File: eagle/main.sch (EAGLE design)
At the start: 15 parts, among them Q1 IRF540, Q2 IRF540

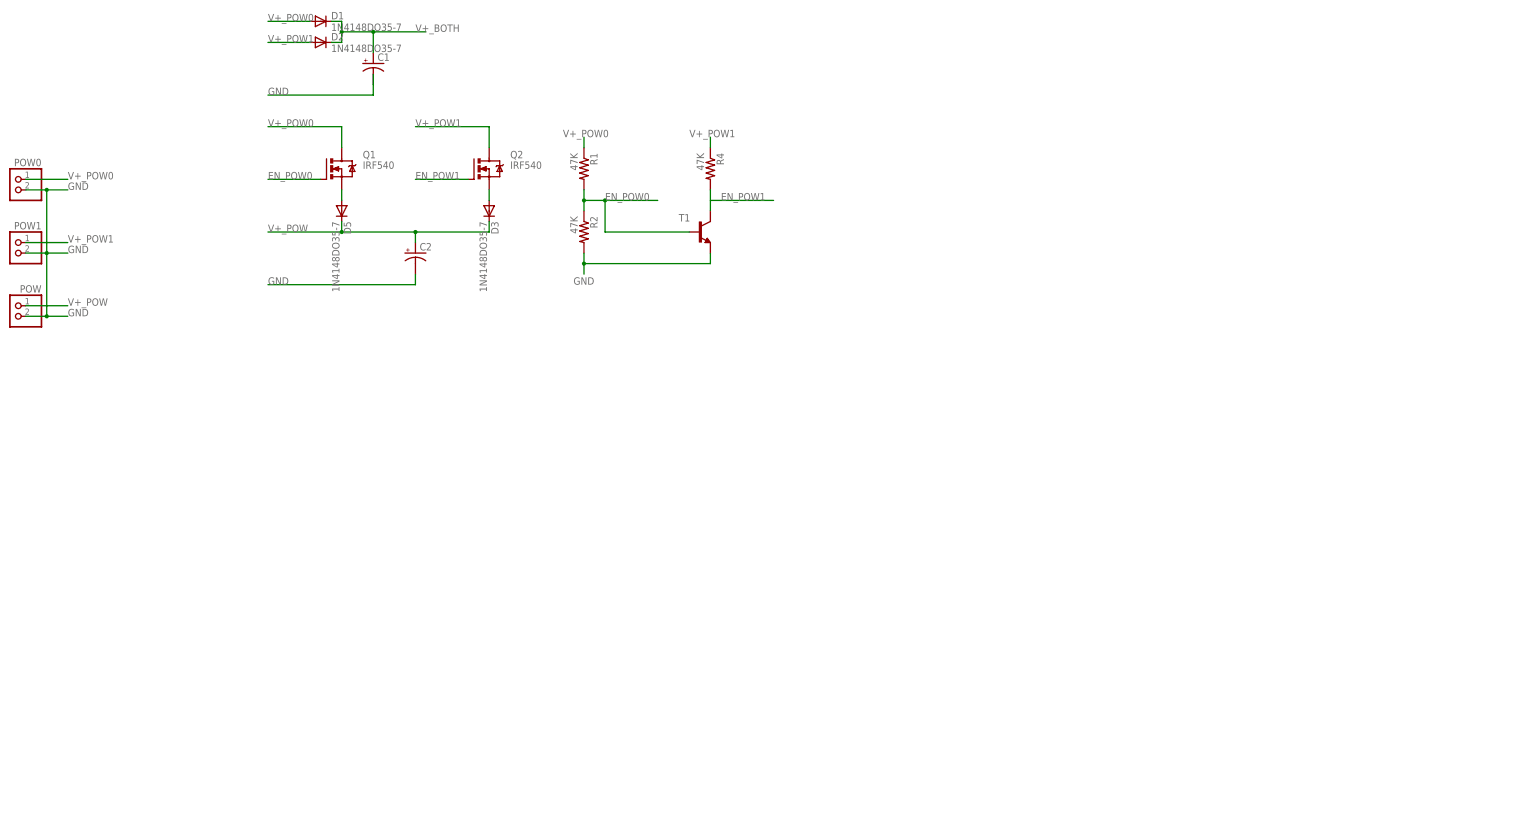
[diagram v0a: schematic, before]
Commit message: update schematic
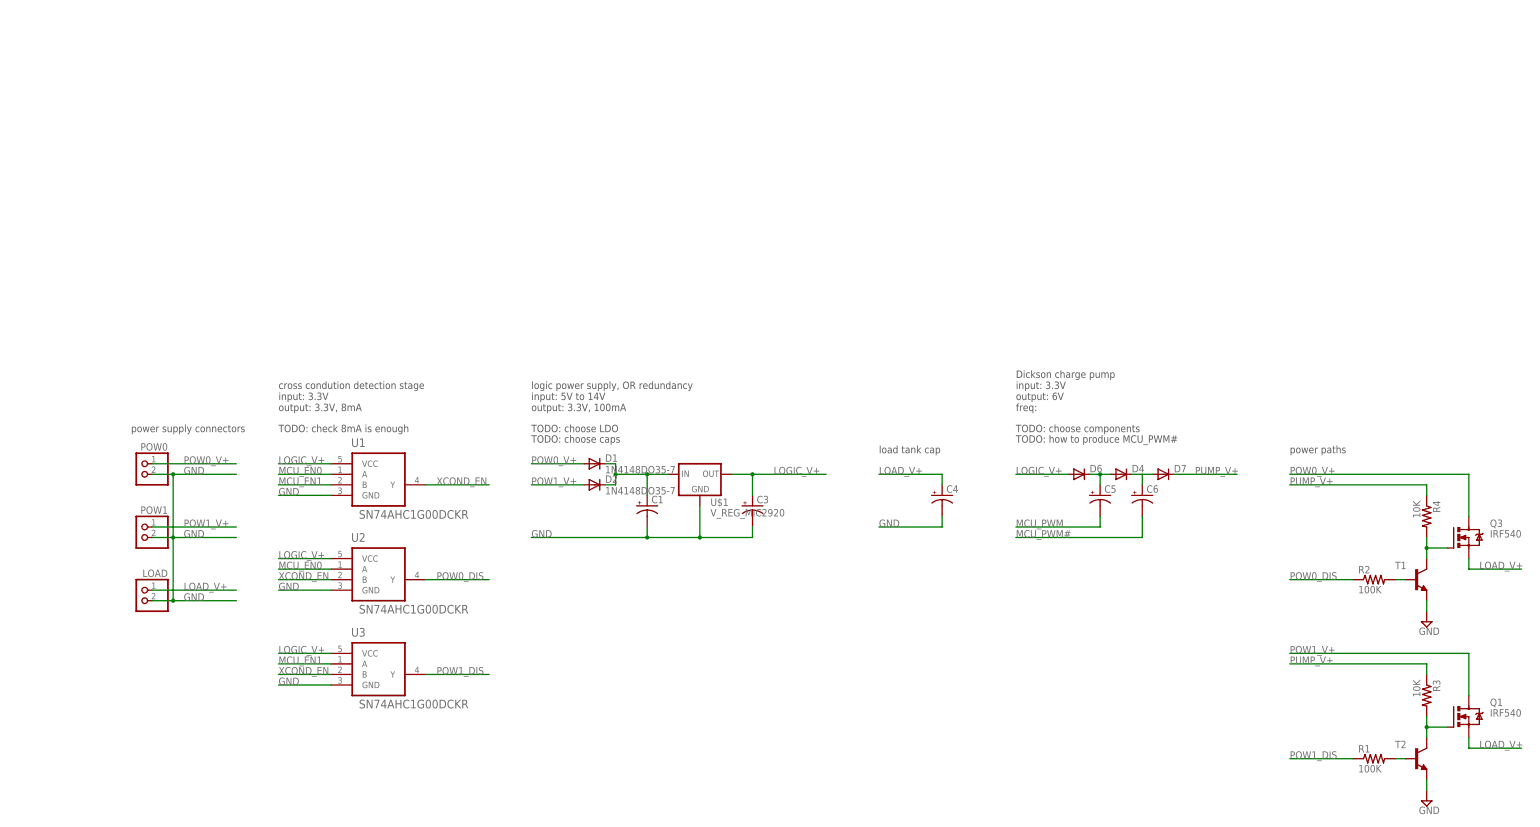
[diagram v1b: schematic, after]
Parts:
- removed C2: (no value), rcl:CPOL-US085CS-1AR
- removed D3, D5: 1N4148DO35-7, diode:1N4148DO35-7
- removed POW: (no value), pinhead:PINHD-1X2
- removed Q2: IRF540, transistor-power:IRF540
- added C3, C4, C5, C6: (no value), rcl:CPOL-US085CS-1AR
- added D4, D6, D7: 1N4148DO35-7, diode:1N4148DO35-7
- added LOAD: (no value), pinhead:PINHD-1X2
- added Q3: IRF540, transistor-power:IRF540
- added R3: 10K, resistor:R-US_0204/2V
- added T2: (no value), transistor:-NPN-TO92
- added U$1: V_REG_MIC2920, SparkFun:V_REG_MIC2920
- added U1, U2, U3: SN74AHC1G00DCKR, TI-SN74AHC1G00DCKR@E:SN74AHC1G00DCKR
- R1, R2: value 47K -> 100K
- R4: value 47K -> 10K
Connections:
- removed net EN_POW0: Q1.G, R1.2, R2.1, T1.B
- removed net EN_POW1: Q2.G
- removed net V+_POW: C2.+, D3.C, D5.C, POW.1
- removed net V+_POW0: D1.A, POW0.1, Q1.D, R1.1
- removed net V+_POW1: D2.A, POW1.1, Q2.D, R4.1
- new net LOAD_V+: C4.+, LOAD.1, Q1.S, Q3.S
- new net LOGIC_V+: C3.+, D6.A, U$1.OUT, U1.VCC, U2.VCC, U3.VCC
- new net MCU_EN0: U1.A, U2.A
- new net MCU_EN1: U1.B, U3.A
- new net MCU_PWM: C5.-
- new net MCU_PWM#: C6.-
- new net N$4: C5.+, D4.A, D6.C
- new net N$5: C6.+, D4.C, D7.A
- new net N$6: R2.2, T1.B
- new net POW0_DIS: R2.1, U2.Y
- new net POW0_V+: D1.A, POW0.1, Q3.D
- new net POW1_DIS: R1.1, U3.Y
- new net POW1_V+: D2.A, POW1.1, Q1.D
- new net PUMP_V+: D7.C, R3.1, R4.1
- new net XCOND_EN: U1.Y, U2.B, U3.B
- net GND: now also C3.-, C4.-, LOAD.2, T2.E, U$1.GND, U1.GND, U2.GND, U3.GND; no longer C2.-, POW.2, R2.2
- net N$1: now also Q3.G
- net N$2: now also Q1.G, R3.2, T2.C; no longer D5.A, Q1.S
- net N$3: now also R1.2, T2.B; no longer D3.A, Q2.S
- net V+_BOTH: now also U$1.IN
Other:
- note added: "Dickson charge pump input: 3.3V output: 6V freq:"
- note added: "TODO: check 8mA is enough"
- note added: "TODO: choose LDO"
- note added: "TODO: choose caps"
- note added: "TODO: choose components"
- note added: "TODO: how to produce MCU_PWM#"
- note added: "cross condution detection stage input: 3.3V output: 3.3V, 8mA"
- note added: "load tank cap"
- note added: "logic power supply, OR redundancy input: 5V to 14V output: 3.3V, 100mA"
- note added: "power paths"
- note added: "power supply connectors"
- moved on the sheet: C1, D1, D2, POW0, POW1, Q1, R1, R2, R4, T1

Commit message: update schematics
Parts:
- added D3: 1N4148DO35-7, diode:1N4148DO35-7
- added R5, R7: 50K, resistor:R-US_0204/2V
- added R6, R8: 10K, resistor:R-US_0204/2V
- added SPI_CON: (no value), pinhead:PINHD-1X6
- added U$2: TEENSY_3.0_ALLPINS, Teensy3.0:TEENSY_3.0_ALLPINS
- renumbered LOAD to LOAD_CON, POW0 to POW0_CON, POW1 to POW1_CON
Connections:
- net MCU_PWM# renamed PUMP_PWM#
- removed net MCU_PWM: C5.-
- removed net V+_BOTH: C1.+, D1.C, D2.C, U$1.IN
- new net MCU_ADC0: U$2.15/A1
- new net MCU_ADC1: U$2.16/A2
- new net MCU_V+: U$2.3.3V, U1.VCC, U2.VCC, U3.VCC
- new net POW01_V+: C1.+, D1.C, D2.C, D6.A, U$1.IN
- new net POW0_VMON: R5.2, R6.1, U$2.11, U$2.23/A9, U$2.3
- new net POW1_VMON: R7.2, R8.1, U$2.12, U$2.4, U$2.9
- new net PUMP_PWM: C5.-, U$2.22/A8
- new net SPI_CS: SPI_CON.2, U$2.2
- new net SPI_MISO: SPI_CON.3, U$2.8
- new net SPI_MOSI: SPI_CON.4, U$2.7
- new net SPI_SCK: SPI_CON.5, U$2.14/A0
- new net SPI_V+: D3.C, SPI_CON.6
- net GND: now also R6.2, R8.2, SPI_CON.1, U$2.GND
- net LOGIC_V+: now also D3.A, U$2.VIN; no longer D6.A, U1.VCC, U2.VCC, U3.VCC
- net POW0_DIS: now also U$2.0
- net POW0_V+: now also R5.1
- net POW1_DIS: now also U$2.1
- net POW1_V+: now also R7.1
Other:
- note added: "Dickson charge pump output: input + 5V freq:"
- note added: "TODO: 6:1 amplifier based stage"
- note added: "TODO: choose diodes"
- note added: "logic power supply, OR redundancy input: 5V to 14V output: 3.7V, 100mA"
- note added: "voltage monitoring paths"
- note removed: "Dickson charge pump input: 3.3V output: 6V freq:"
- note removed: "logic power supply, OR redundancy input: 5V to 14V output: 3.3V, 100mA"

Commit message: PWM#
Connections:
- net PUMP_PWM#: now also U$2.21/A7
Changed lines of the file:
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@@
 <label x="254" y="-17.78" size="1.778" layer="95"/>
+</segment>
+<segment>
+<pinref part="U$2" gate="G$1" pin="21/A7"/>
+<wire x1="226.06" y1="-121.92" x2="243.84" y2="-121.92" width="0.1524" layer="91"/>
+<label x="228.6" y="-121.92" size="1.778" layer="95"/>
 </segment>
 </net>

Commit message: update schematics
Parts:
- removed U$1: V_REG_MIC2920, SparkFun:V_REG_MIC2920
- added C2: 470p, resistor:C-EU025-024X044
- added IC1: TS5205, v-reg:TS5205
- added U6: OPA2340UA, TI-OPA2340UA:OPA2340UA
- C3: value (none) -> 2.2u
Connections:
- new net N$8: C2.1, IC1.CB
- net GND: now also C2.2, IC1.GND; no longer U$1.GND
- net LOGIC_V+: now also IC1.VOUT; no longer U$1.OUT
- net POW01_V+: now also IC1.CE, IC1.VIN; no longer U$1.IN
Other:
- note added: "TODO: 5:1 amplifier based stage"
- note added: "TODO: choose LDO 4V"
- note added: "logic power supply, OR redundancy input: 5V to 16V output: 4V, 150mA"
- note removed: "TODO: 6:1 amplifier based stage"
- note removed: "TODO: choose LDO"
- note removed: "logic power supply, OR redundancy input: 5V to 14V output: 3.7V, 100mA"
- moved on the sheet: C1, C3, C4, D3
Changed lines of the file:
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@@
 <part name="U2" library="TI-SN74AHC1G00DCKR@E" deviceset="SN74AHC1G00DCKR" device=""/>
 <part name="U3" library="TI-SN74AHC1G00DCKR@E" deviceset="SN74AHC1G00DCKR" device=""/>
-<part name="U$1" library="SparkFun" deviceset="V_REG_MIC2920" device=""/>
-<part name="C3" library="rcl" deviceset="CPOL-US" device="085CS-1AR"/>
+<part name="C3" library="rcl" deviceset="CPOL-US" device="085CS-1AR" value="2.2u"/>
 <part name="C4" library="rcl" deviceset="CPOL-US" device="085CS-1AR"/>
 <part name="D4" library="diode" deviceset="1N4148" device="DO35-7"/>
@@
 <part name="R8" library="resistor" deviceset="R-US_" device="0204/2V" value="10K"/>
 <part name="SUPPLY4" library="supply2" deviceset="GND" device=""/>
+<part name="IC1" library="v-reg" deviceset="TS5205" device=""/>
+<part name="C2" library="resistor" deviceset="C-EU" device="025-024X044" value="470p"/>
+<part name="U6" library="TI-OPA2340UA" deviceset="OPA2340UA" device=""/>
 </parts>
 <sheets>
@@
 <text x="40.64" y="7.62" size="1.778" layer="97">power supply connectors</text>
 <text x="137.16" y="15.24" size="1.778" layer="97">logic power supply, OR redundancy
-input: 5V to 14V
-output: 3.7V, 100mA</text>
-<text x="137.16" y="10.16" size="1.778" layer="97">TODO: choose LDO</text>
+input: 5V to 16V
+output: 4V, 150mA</text>
+<text x="137.16" y="10.16" size="1.778" layer="97">TODO: choose LDO 4V</text>
 <text x="137.16" y="7.62" size="1.778" layer="97">TODO: choose caps</text>
-<text x="220.98" y="2.54" size="1.778" layer="97">load tank cap</text>
+<text x="226.06" y="10.16" size="1.778" layer="97">load tank cap</text>
 <text x="254" y="12.7" size="1.778" layer="97">Dickson charge pump
 output: input + 5V
@@
 <text x="137.16" y="5.08" size="1.778" layer="97">TODO: choose diodes</text>
 <text x="391.16" y="7.62" size="1.778" layer="97">voltage monitoring paths</text>
-<text x="391.16" y="2.54" size="1.778" layer="97">TODO: 6:1 amplifier based stage</text>
+<text x="391.16" y="2.54" size="1.778" layer="97">TODO: 5:1 amplifier based stage</text>
 </plain>
 <instances>
@@
 <attribute name="NAME" x="154.94" y="-4.5974" size="1.778" layer="95"/>
 </instance>
-<instance part="C1" gate="G$1" x="165.1" y="-10.16"/>
+<instance part="C1" gate="G$1" x="162.56" y="-10.16"/>
 <instance part="R2" gate="G$1" x="340.36" y="-27.94"/>
 <instance part="T1" gate="G$1" x="350.52" y="-27.94" smashed="yes">
@@
 <instance part="U2" gate="A" x="93.98" y="-33.02"/>
 <instance part="U3" gate="A" x="93.98" y="-55.88"/>
-<instance part="U$1" gate="G$1" x="177.8" y="-2.54"/>
-<instance part="C3" gate="G$1" x="190.5" y="-10.16"/>
-<instance part="C4" gate="G$1" x="236.22" y="-7.62"/>
+<instance part="C3" gate="G$1" x="203.2" y="-10.16"/>
+<instance part="C4" gate="G$1" x="241.3" y="0"/>
 <instance part="D4" gate="G$1" x="279.4" y="-2.54" smashed="yes">
 <attribute name="NAME" x="281.94" y="-2.0574" size="1.778" layer="95"/>
@@
 <instance part="Q1" gate="G$1" x="360.68" y="-60.96"/>
 <instance part="U$2" gate="G$1" x="210.82" y="-106.68"/>
-<instance part="D3" gate="G$1" x="190.5" y="2.54" smashed="yes">
-<attribute name="NAME" x="193.04" y="3.0226" size="1.778" layer="95"/>
+<instance part="D3" gate="G$1" x="200.66" y="10.16" smashed="yes">
+<attribute name="NAME" x="203.2" y="10.6426" size="1.778" layer="95"/>
 </instance>
 <instance part="SPI_CON" gate="A" x="43.18" y="-60.96" rot="MR0"/>
@@
 <instance part="R8" gate="G$1" x="408.94" y="-68.58" rot="R270"/>
 <instance part="SUPPLY4" gate="GND" x="408.94" y="-78.74"/>
+<instance part="IC1" gate="G$1" x="180.34" y="0"/>
+<instance part="C2" gate="G$1" x="193.04" y="-10.16"/>
+<instance part="U6" gate="A" x="444.5" y="-15.24"/>
 </instances>
 <busses>
@@
 <segment>
 <pinref part="C1" gate="G$1" pin="-"/>
-<wire x1="165.1" y1="-15.24" x2="165.1" y2="-17.78" width="0.1524" layer="91"/>
-<wire x1="165.1" y1="-17.78" x2="137.16" y2="-17.78" width="0.1524" layer="91"/>
+<wire x1="162.56" y1="-15.24" x2="162.56" y2="-17.78" width="0.1524" layer="91"/>
+<wire x1="162.56" y1="-17.78" x2="137.16" y2="-17.78" width="0.1524" layer="91"/>
 <label x="137.16" y="-17.78" size="1.778" layer="95"/>
-<pinref part="U$1" gate="G$1" pin="GND"/>
-<wire x1="177.8" y1="-10.16" x2="177.8" y2="-17.78" width="0.1524" layer="91"/>
-<wire x1="177.8" y1="-17.78" x2="165.1" y2="-17.78" width="0.1524" layer="91"/>
-<junction x="165.1" y="-17.78"/>
+<junction x="162.56" y="-17.78"/>
+<wire x1="203.2" y1="-17.78" x2="193.04" y2="-17.78" width="0.1524" layer="91"/>
+<pinref part="IC1" gate="G$1" pin="GND"/>
+<wire x1="193.04" y1="-17.78" x2="170.18" y2="-17.78" width="0.1524" layer="91"/>
+<wire x1="170.18" y1="-17.78" x2="162.56" y2="-17.78" width="0.1524" layer="91"/>
+<wire x1="170.18" y1="-5.08" x2="170.18" y2="-17.78" width="0.1524" layer="91"/>
+<junction x="170.18" y="-17.78"/>
 <pinref part="C3" gate="G$1" pin="-"/>
-<wire x1="190.5" y1="-15.24" x2="190.5" y2="-17.78" width="0.1524" layer="91"/>
-<wire x1="190.5" y1="-17.78" x2="177.8" y2="-17.78" width="0.1524" layer="91"/>
-<junction x="177.8" y="-17.78"/>
+<wire x1="203.2" y1="-15.24" x2="203.2" y2="-17.78" width="0.1524" layer="91"/>
+<pinref part="C2" gate="G$1" pin="2"/>
+<wire x1="193.04" y1="-15.24" x2="193.04" y2="-17.78" width="0.1524" layer="91"/>
+<junction x="193.04" y="-17.78"/>
 </segment>
 <segment>
@@
 <segment>
 <pinref part="C4" gate="G$1" pin="-"/>
-<wire x1="236.22" y1="-12.7" x2="236.22" y2="-15.24" width="0.1524" layer="91"/>
-<wire x1="236.22" y1="-15.24" x2="220.98" y2="-15.24" width="0.1524" layer="91"/>
-<label x="220.98" y="-15.24" size="1.778" layer="95"/>
+<wire x1="241.3" y1="-5.08" x2="241.3" y2="-7.62" width="0.1524" layer="91"/>
+<wire x1="241.3" y1="-7.62" x2="226.06" y2="-7.62" width="0.1524" layer="91"/>
+<label x="226.06" y="-7.62" size="1.778" layer="95"/>
 </segment>
 <segment>
@@
 <wire x1="157.48" y1="-2.54" x2="157.48" y2="-5.08" width="0.1524" layer="91"/>
 <wire x1="157.48" y1="-5.08" x2="154.94" y2="-5.08" width="0.1524" layer="91"/>
-<wire x1="157.48" y1="-2.54" x2="165.1" y2="-2.54" width="0.1524" layer="91"/>
+<wire x1="157.48" y1="-2.54" x2="162.56" y2="-2.54" width="0.1524" layer="91"/>
 <junction x="157.48" y="-2.54"/>
 <pinref part="C1" gate="G$1" pin="+"/>
-<wire x1="165.1" y1="-2.54" x2="165.1" y2="-7.62" width="0.1524" layer="91"/>
-<pinref part="U$1" gate="G$1" pin="IN"/>
-<wire x1="165.1" y1="-2.54" x2="170.18" y2="-2.54" width="0.1524" layer="91"/>
-<junction x="165.1" y="-2.54"/>
+<wire x1="162.56" y1="-2.54" x2="162.56" y2="-7.62" width="0.1524" layer="91"/>
 <wire x1="157.48" y1="-5.08" x2="157.48" y2="-10.16" width="0.1524" layer="91"/>
 <junction x="157.48" y="-5.08"/>
 <wire x1="157.48" y1="-10.16" x2="137.16" y2="-10.16" width="0.1524" layer="91"/>
 <label x="137.16" y="-10.16" size="1.778" layer="95"/>
+<wire x1="162.56" y1="-2.54" x2="162.56" y2="0" width="0.1524" layer="91"/>
+<junction x="162.56" y="-2.54"/>
+<pinref part="IC1" gate="G$1" pin="VIN"/>
+<wire x1="162.56" y1="0" x2="162.56" y2="5.08" width="0.1524" layer="91"/>
+<wire x1="162.56" y1="5.08" x2="170.18" y2="5.08" width="0.1524" layer="91"/>
+<pinref part="IC1" gate="G$1" pin="CE"/>
+<wire x1="170.18" y1="0" x2="162.56" y2="0" width="0.1524" layer="91"/>
+<junction x="162.56" y="0"/>
 </segment>
 <segment>
@@
 <net name="LOGIC_V+" class="0">
 <segment>
-<pinref part="U$1" gate="G$1" pin="OUT"/>
-<wire x1="185.42" y1="-2.54" x2="190.5" y2="-2.54" width="0.1524" layer="91"/>
+<wire x1="193.04" y1="5.08" x2="203.2" y2="5.08" width="0.1524" layer="91"/>
+<label x="203.2" y="5.08" size="1.778" layer="95"/>
+<pinref part="D3" gate="G$1" pin="A"/>
+<wire x1="203.2" y1="5.08" x2="215.9" y2="5.08" width="0.1524" layer="91"/>
+<wire x1="198.12" y1="10.16" x2="193.04" y2="10.16" width="0.1524" layer="91"/>
+<wire x1="193.04" y1="10.16" x2="193.04" y2="5.08" width="0.1524" layer="91"/>
+<pinref part="IC1" gate="G$1" pin="VOUT"/>
+<wire x1="190.5" y1="5.08" x2="193.04" y2="5.08" width="0.1524" layer="91"/>
+<junction x="193.04" y="5.08"/>
 <pinref part="C3" gate="G$1" pin="+"/>
-<wire x1="190.5" y1="-2.54" x2="208.28" y2="-2.54" width="0.1524" layer="91"/>
-<wire x1="190.5" y1="-7.62" x2="190.5" y2="-2.54" width="0.1524" layer="91"/>
-<junction x="190.5" y="-2.54"/>
-<label x="195.58" y="-2.54" size="1.778" layer="95"/>
-<pinref part="D3" gate="G$1" pin="A"/>
-<wire x1="187.96" y1="2.54" x2="185.42" y2="2.54" width="0.1524" layer="91"/>
-<wire x1="185.42" y1="2.54" x2="185.42" y2="-2.54" width="0.1524" layer="91"/>
-<junction x="185.42" y="-2.54"/>
+<wire x1="203.2" y1="5.08" x2="203.2" y2="-7.62" width="0.1524" layer="91"/>
+<junction x="203.2" y="5.08"/>
 </segment>
 <segment>
@@
 <segment>
 <pinref part="C4" gate="G$1" pin="+"/>
-<wire x1="236.22" y1="-5.08" x2="236.22" y2="-2.54" width="0.1524" layer="91"/>
-<wire x1="236.22" y1="-2.54" x2="220.98" y2="-2.54" width="0.1524" layer="91"/>
-<label x="220.98" y="-2.54" size="1.778" layer="95"/>
+<wire x1="241.3" y1="2.54" x2="241.3" y2="5.08" width="0.1524" layer="91"/>
+<wire x1="241.3" y1="5.08" x2="226.06" y2="5.08" width="0.1524" layer="91"/>
+<label x="226.06" y="5.08" size="1.778" layer="95"/>
 </segment>
 <segment>
@@
 <segment>
 <pinref part="D3" gate="G$1" pin="C"/>
-<wire x1="193.04" y1="2.54" x2="208.28" y2="2.54" width="0.1524" layer="91"/>
-<label x="198.12" y="2.54" size="1.778" layer="95"/>
+<wire x1="203.2" y1="10.16" x2="215.9" y2="10.16" width="0.1524" layer="91"/>
+<label x="208.28" y="10.16" size="1.778" layer="95"/>
 </segment>
 <segment>
@@
 </segment>
 </net>
+<net name="N$8" class="0">
+<segment>
+<pinref part="IC1" gate="G$1" pin="CB"/>
+<wire x1="190.5" y1="-2.54" x2="193.04" y2="-2.54" width="0.1524" layer="91"/>
+<pinref part="C2" gate="G$1" pin="1"/>
+<wire x1="193.04" y1="-2.54" x2="193.04" y2="-7.62" width="0.1524" layer="91"/>
+</segment>
+</net>

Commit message: update schematics
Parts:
- R5, R7: value 50K -> 400K
- R6, R8: value 10K -> 100K
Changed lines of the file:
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@@
 <part name="D3" library="diode" deviceset="1N4148" device="DO35-7"/>
 <part name="SPI_CON" library="pinhead" deviceset="PINHD-1X6" device=""/>
-<part name="R5" library="resistor" deviceset="R-US_" device="0204/2V" value="50K"/>
-<part name="R6" library="resistor" deviceset="R-US_" device="0204/2V" value="10K"/>
+<part name="R5" library="resistor" deviceset="R-US_" device="0204/2V" value="400K"/>
+<part name="R6" library="resistor" deviceset="R-US_" device="0204/2V" value="100K"/>
 <part name="SUPPLY3" library="supply2" deviceset="GND" device=""/>
-<part name="R7" library="resistor" deviceset="R-US_" device="0204/2V" value="50K"/>
-<part name="R8" library="resistor" deviceset="R-US_" device="0204/2V" value="10K"/>
+<part name="R7" library="resistor" deviceset="R-US_" device="0204/2V" value="400K"/>
+<part name="R8" library="resistor" deviceset="R-US_" device="0204/2V" value="100K"/>
 <part name="SUPPLY4" library="supply2" deviceset="GND" device=""/>
 <part name="IC1" library="v-reg" deviceset="TS5205" device=""/>

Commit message: update
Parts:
- removed Q3: IRF540, transistor-power:IRF540
- removed U6: OPA2340UA, TI-OPA2340UA:OPA2340UA
- added Q5: SI4840DY, transistor-fet:SI4840DY
- Q1: value IRF540 -> SI4840DY; device transistor-power:IRF540 -> transistor-fet:SI4840DY
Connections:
- removed net MCU_EN0: U1.A, U2.A
- removed net MCU_EN1: U1.B, U3.A
- new net POW0_EN: U$2.0, U1.A, U2.A
- new net POW1_EN: U$2.1, U1.B, U3.A
- net LOAD_V+: now also Q5.S; no longer Q3.S
- net MCU_ADC0: now also U$2.18/A4; no longer U$2.15/A1
- net MCU_ADC1: now also U$2.19/A5; no longer U$2.16/A2
- net N$1: now also Q5.G; no longer Q3.G
- net POW0_DIS: no longer U$2.0
- net POW0_V+: now also Q5.D; no longer Q3.D
- net POW1_DIS: no longer U$2.1
- net PUMP_PWM: now also U$2.16/A2; no longer U$2.22/A8
- net PUMP_PWM#: now also U$2.17/A3; no longer U$2.21/A7
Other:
- note added: "SI4166DY"
- note added: "SPI connector"
- note added: "TODO: choose FET"
- note added: "TODO: choose Schottky diodes"
- note added: "TODO: choose connectors"
- note added: "TODO: choose resistors"
- note added: "cross condution detection stage input: 3.3V output: 3.3V, 8mA EN0 EN1 XEN DIS0 DIS1 0 0 1 1 1 0 1 1 1 0 1 0 1 0 1 1 1 0 1 1"
- note removed: "TODO: 5:1 amplifier based stage"
- note removed: "TODO: check 8mA is enough"
- note removed: "TODO: choose LDO 4V"
- note removed: "TODO: choose components"
- note removed: "TODO: how to produce MCU_PWM#"
- note removed: "cross condution detection stage input: 3.3V output: 3.3V, 8mA"
- moved on the sheet: U$2
